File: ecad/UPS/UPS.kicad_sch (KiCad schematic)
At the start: 0 parts

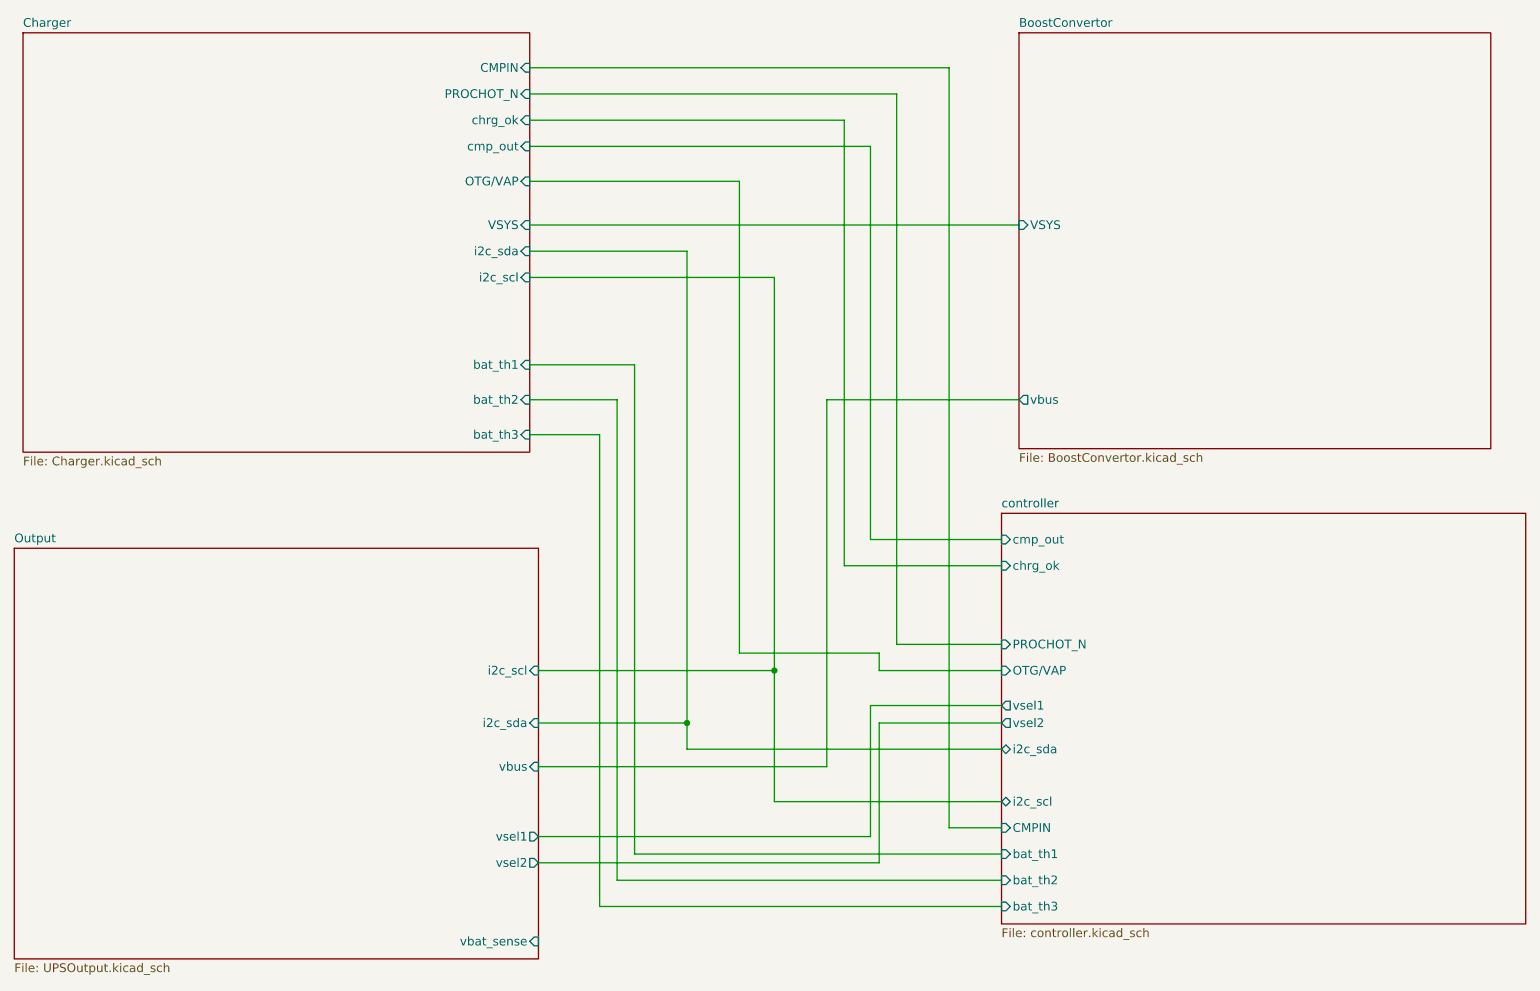
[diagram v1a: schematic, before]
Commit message: Got VBAT_SENSE labels fixed, wasn't a sheet pin for some reason
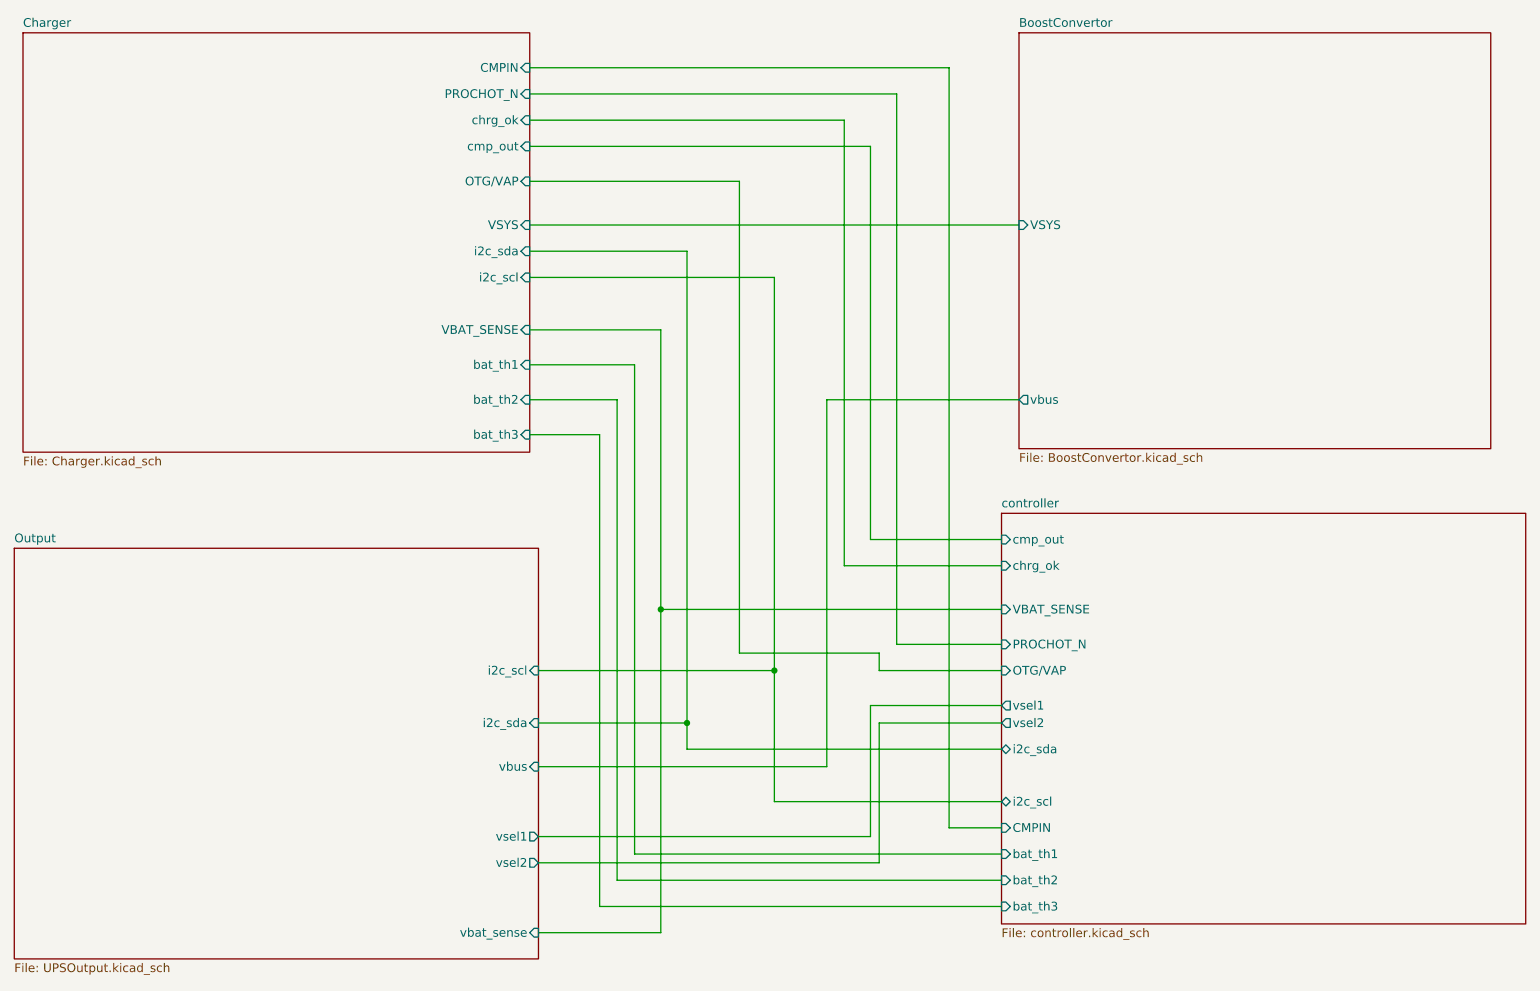
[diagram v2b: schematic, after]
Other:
- sheet Charger ports: added VBAT_SENSE; removed none
- sheet controller ports: added VBAT_SENSE; removed none
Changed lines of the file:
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@@
+	)
+	(junction
+		(at 118.11 110.49)
+		(diameter 0)
+		(color 0 0 0 0)
 	)
 	(junction
@@
 	(wire
 		(pts
+			(xy 100.33 157.48) (xy 118.11 157.48)
+		)
+		(stroke
+			(width 0)
+			(type default)
+		)
+	)
+	(wire
+		(pts
 			(xy 149.86 127) (xy 149.86 147.32)
 		)
@@
 	(wire
 		(pts
+			(xy 118.11 69.85) (xy 99.06 69.85)
+		)
+		(stroke
+			(width 0)
+			(type default)
+		)
+	)
+	(wire
+		(pts
 			(xy 99.06 48.26) (xy 129.54 48.26)
 		)
@@
 	(wire
 		(pts
+			(xy 118.11 157.48) (xy 118.11 110.49)
+		)
+		(stroke
+			(width 0)
+			(type default)
+		)
+	)
+	(wire
+		(pts
+			(xy 118.11 110.49) (xy 118.11 69.85)
+		)
+		(stroke
+			(width 0)
+			(type default)
+		)
+	)
+	(wire
+		(pts
 			(xy 114.3 74.93) (xy 114.3 146.05)
 		)
@@
 		(pts
 			(xy 142.24 80.01) (xy 142.24 133.35)
+		)
+		(stroke
+			(width 0)
+			(type default)
+		)
+	)
+	(wire
+		(pts
+			(xy 167.64 110.49) (xy 118.11 110.49)
 		)
 		(stroke
@@
 			)
 		)
+		(pin "VBAT_SENSE" input
+			(at 167.64 110.49 180)
+			(effects
+				(font
+					(size 1.27 1.27)
+				)
+				(justify left)
+			)
+		)
 		(instances
 			(project "UPS"
@@
 			)
 		)
+		(pin "VBAT_SENSE" input
+			(at 99.06 69.85 0)
+			(effects
+				(font
+					(size 1.27 1.27)
+				)
+				(justify right)
+			)
+		)
 		(instances
 			(project "UPS"
@@
 			)
 		)
-		(pin "vbat_sense" input
-			(at 100.33 158.75 0)
-			(effects
-				(font
-					(size 1.27 1.27)
-				)
-				(justify right)
-			)
-		)
 		(pin "vsel1" output
 			(at 100.33 143.51 0)
@@
 			(effects
 				(font
+					(size 1.27 1.27)
+				)
+				(justify right)
+			)
+		)
+		(pin "vbat_sense" input
+			(at 100.33 157.48 0)
+			(effects
+				(font

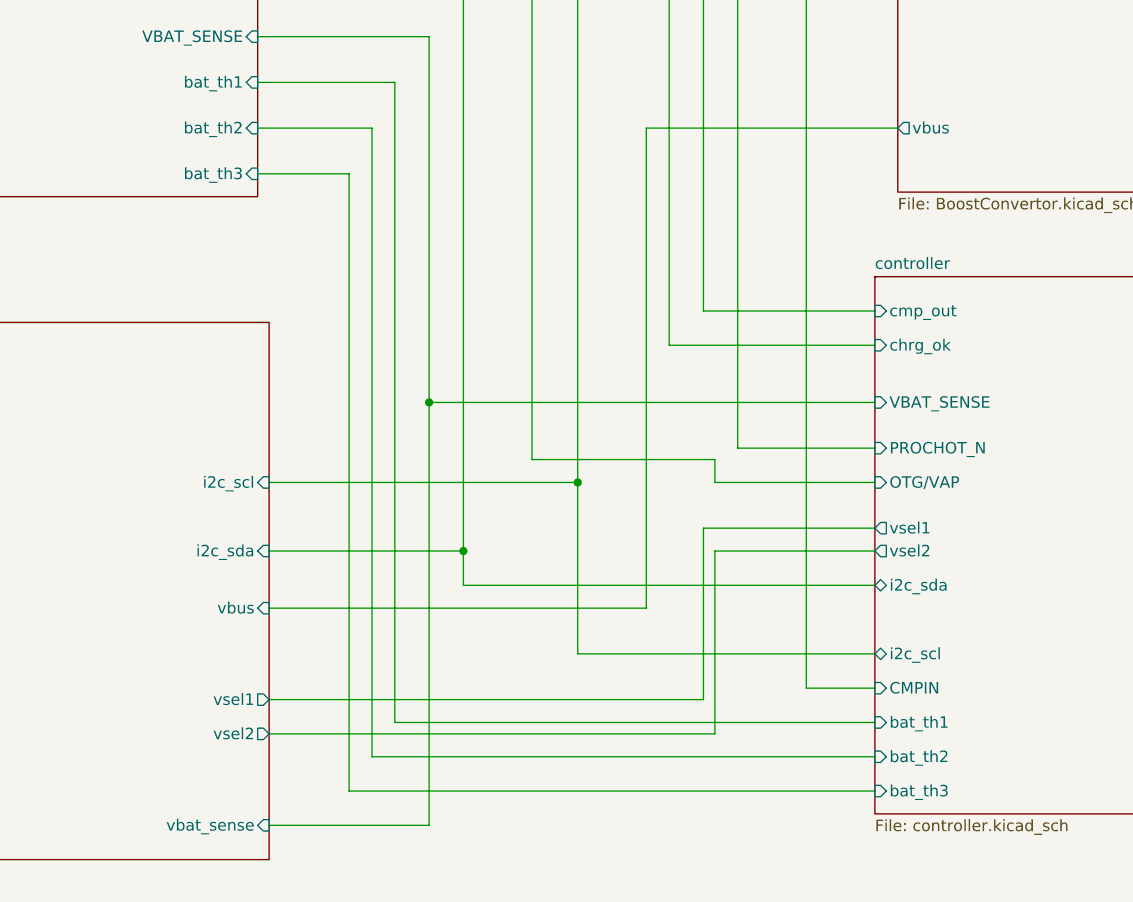
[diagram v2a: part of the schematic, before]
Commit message: touches
Add battery and board thermistor circuits on PC0/PC1.

Implement ADC sampling, temperature conversion, and sensor fault reporting.

Enable the STM32 ADC drivers and poll temperatures in the main loop.

Add the OLED connector on PB10/PB11 and update PCB footprints and net assignments.

Add a Raspberry Pi mounting-hole footprint.

Exclude local docs and test folders from Git.

five ADC sensor inputs

fan-control logic.
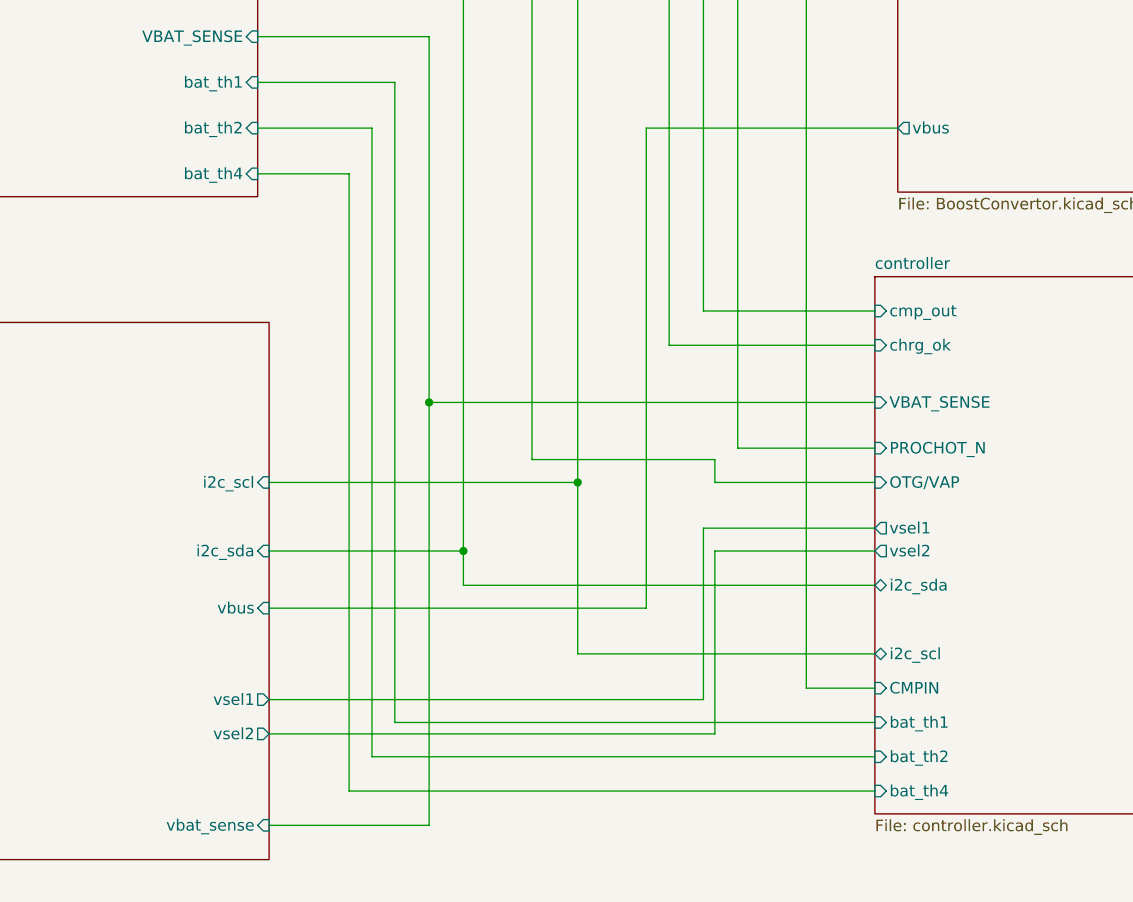
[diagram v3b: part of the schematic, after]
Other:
- sheet Charger ports: added bat_th4; removed bat_th3
- sheet controller ports: added bat_th4; removed bat_th3
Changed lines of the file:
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@@
 			)
 		)
-		(pin "bat_th3" input
+		(pin "bat_th4" input
 			(at 167.64 153.67 180)
 			(effects
@@
 			)
 		)
-		(pin "bat_th3" input
+		(pin "bat_th4" input
 			(at 99.06 85.09 0)
 			(effects

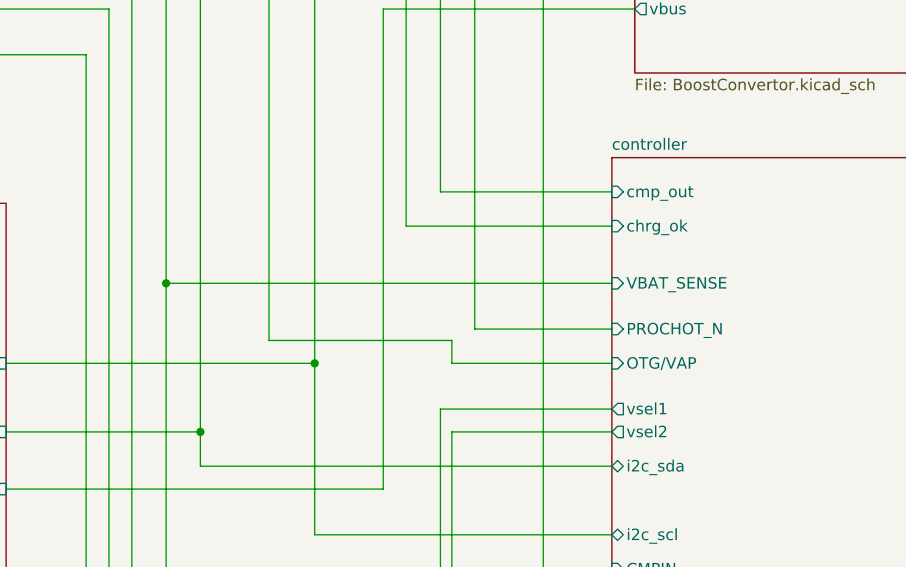
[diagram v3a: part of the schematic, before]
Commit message: more stuff to route yay!
uart for the pi5
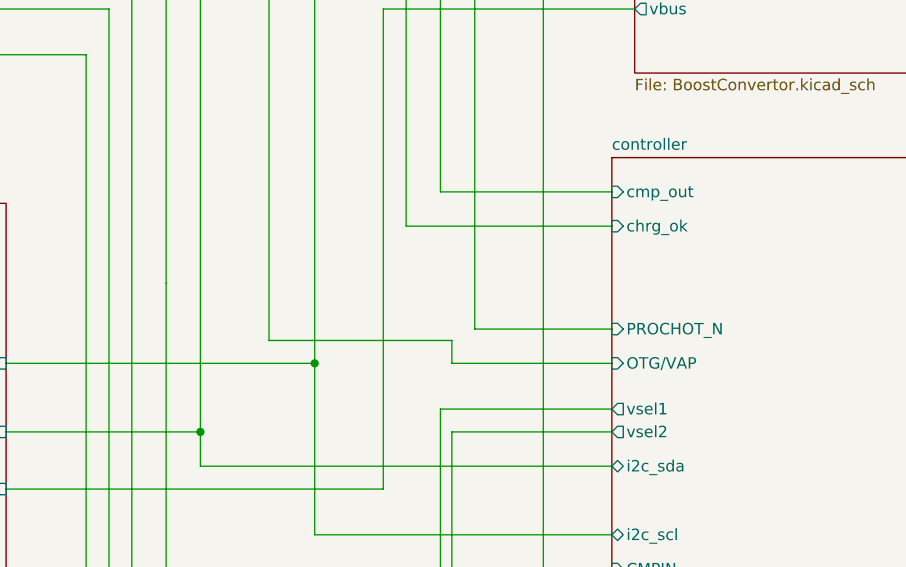
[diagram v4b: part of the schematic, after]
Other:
- sheet controller ports: added none; removed VBAT_SENSE
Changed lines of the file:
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@@
-	)
-	(junction
-		(at 118.11 110.49)
-		(diameter 0)
-		(color 0 0 0 0)
 	)
 	(junction
@@
 		(pts
 			(xy 142.24 80.01) (xy 142.24 133.35)
-		)
-		(stroke
-			(width 0)
-			(type default)
-		)
-	)
-	(wire
-		(pts
-			(xy 167.64 110.49) (xy 118.11 110.49)
 		)
 		(stroke
@@
 			(effects
 				(font
-					(size 1.27 1.27)
-				)
-				(justify left)
-			)
-		)
-		(pin "VBAT_SENSE" input
-			(at 167.64 110.49 180)
-			(effects
-				(font
